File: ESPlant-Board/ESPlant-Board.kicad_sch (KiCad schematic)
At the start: 47 parts, among them J1 Conn_01x05, U1 USB-C, U13 ESP32-C6-MINI-1-N4, U3 AHT20-F, U4 Tactile-Switch, U5 3.3V-Regulator, U6 Light sensor, U7 Tactile-Switch, U8 Slide-Switch, U9 Battery-Spring

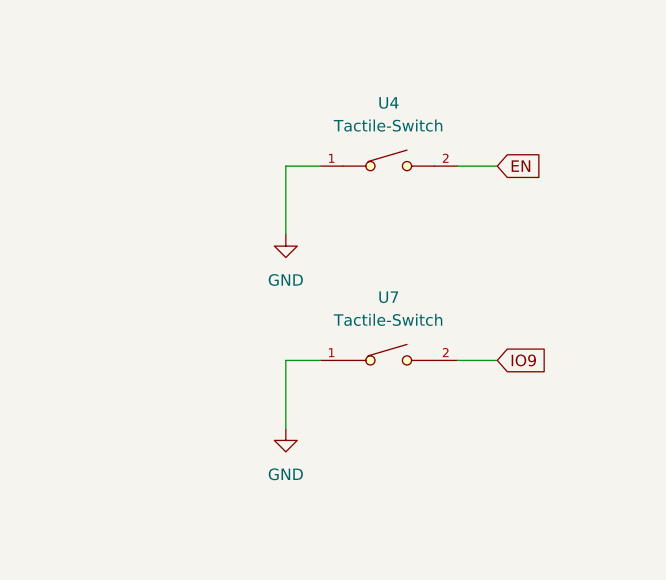
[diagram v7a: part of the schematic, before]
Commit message: Board: Add debouncing caps to buttons
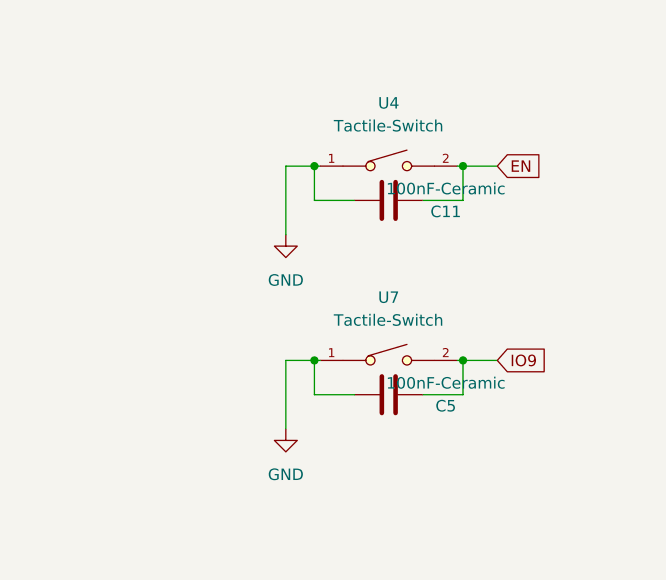
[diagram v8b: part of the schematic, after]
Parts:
- added C11, C5: 100nF-Ceramic, Capacitor_SMD:C_0402_1005Metric, symbol Device:C
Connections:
- net EN: now also C11.1
- net GND: now also C11.2, C5.2
- net IO9: now also C5.1
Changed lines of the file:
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@@
   (junction (at 205.74 81.28) (diameter 0) (color 0 0 0 0)
   )
+  (junction (at 254.635 99.06) (diameter 0) (color 0 0 0 0)
+  )
   (junction (at 205.74 101.6) (diameter 0) (color 0 0 0 0)
   )
@@
   (junction (at 93.345 165.735) (diameter 0) (color 0 0 0 0)
   )
+  (junction (at 254.635 77.47) (diameter 0) (color 0 0 0 0)
+  )
   (junction (at 36.83 175.895) (diameter 0) (color 0 0 0 0)
   )
@@
   (junction (at 31.115 175.895) (diameter 0) (color 0 0 0 0)
   )
+  (junction (at 271.145 99.06) (diameter 0) (color 0 0 0 0)
+  )
   (junction (at 36.83 168.275) (diameter 0) (color 0 0 0 0)
   )
@@
   )
   (junction (at 205.74 99.06) (diameter 0) (color 0 0 0 0)
+  )
+  (junction (at 271.145 77.47) (diameter 0) (color 0 0 0 0)
   )
   (junction (at 70.485 111.76) (diameter 0) (color 0 0 0 0)
@@
     (stroke (width 0) (type default))
   )
+  (wire (pts (xy 271.145 102.87) (xy 271.145 99.06))
+    (stroke (width 0) (type default))
+  )
   (wire (pts (xy 205.74 99.06) (xy 205.74 101.6))
     (stroke (width 0) (type default))
@@
     (stroke (width 0) (type default))
   )
-  (wire (pts (xy 270.51 77.47) (xy 274.955 77.47))
+  (wire (pts (xy 270.51 77.47) (xy 271.145 77.47))
     (stroke (width 0) (type default))
   )
@@
     (stroke (width 0) (type default))
   )
+  (wire (pts (xy 254.635 99.06) (xy 255.27 99.06))
+    (stroke (width 0) (type default))
+  )
   (wire (pts (xy 128.905 188.595) (xy 129.54 188.595))
     (stroke (width 0) (type default))
@@
     (stroke (width 0) (type default))
   )
+  (wire (pts (xy 271.145 81.28) (xy 271.145 77.47))
+    (stroke (width 0) (type default))
+  )
   (wire (pts (xy 252.73 17.78) (xy 256.54 17.78))
     (stroke (width 0) (type default))
@@
     (stroke (width 0) (type default))
   )
+  (wire (pts (xy 254.635 102.87) (xy 254.635 99.06))
+    (stroke (width 0) (type default))
+  )
   (wire (pts (xy 165.1 55.245) (xy 163.83 55.245))
     (stroke (width 0) (type default))
@@
     (stroke (width 0) (type default))
   )
+  (wire (pts (xy 254.635 81.28) (xy 254.635 77.47))
+    (stroke (width 0) (type default))
+  )
   (wire (pts (xy 128.905 173.355) (xy 129.54 173.355))
     (stroke (width 0) (type default))
@@
     (stroke (width 0) (type default))
   )
+  (wire (pts (xy 271.145 77.47) (xy 274.955 77.47))
+    (stroke (width 0) (type default))
+  )
   (wire (pts (xy 64.77 24.13) (xy 64.77 34.29))
     (stroke (width 0) (type default))
@@
     (stroke (width 0) (type default))
   )
+  (wire (pts (xy 271.145 99.06) (xy 274.955 99.06))
+    (stroke (width 0) (type default))
+  )
   (wire (pts (xy 123.825 168.275) (xy 150.495 168.275))
     (stroke (width 0) (type default))
@@
     (stroke (width 0) (type default))
   )
+  (wire (pts (xy 266.7 81.28) (xy 271.145 81.28))
+    (stroke (width 0) (type default))
+  )
+  (wire (pts (xy 259.08 81.28) (xy 254.635 81.28))
+    (stroke (width 0) (type default))
+  )
   (wire (pts (xy 150.495 165.735) (xy 128.905 165.735))
     (stroke (width 0) (type default))
@@
     (stroke (width 0) (type default))
   )
+  (wire (pts (xy 266.7 102.87) (xy 271.145 102.87))
+    (stroke (width 0) (type default))
+  )
   (wire (pts (xy 31.115 167.005) (xy 31.115 168.275))
     (stroke (width 0) (type default))
@@
     (stroke (width 0) (type default))
   )
-  (wire (pts (xy 251.46 99.06) (xy 255.27 99.06))
+  (wire (pts (xy 251.46 99.06) (xy 254.635 99.06))
     (stroke (width 0) (type default))
   )
@@
     (stroke (width 0) (type default))
   )
+  (wire (pts (xy 254.635 77.47) (xy 255.27 77.47))
+    (stroke (width 0) (type default))
+  )
   (wire (pts (xy 88.265 180.34) (xy 87.63 180.34))
     (stroke (width 0) (type default))
@@
     (stroke (width 0) (type default))
   )
+  (wire (pts (xy 259.08 102.87) (xy 254.635 102.87))
+    (stroke (width 0) (type default))
+  )
   (wire (pts (xy 74.295 170.815) (xy 74.295 175.895))
     (stroke (width 0) (type default))
@@
     (stroke (width 0) (type default))
   )
-  (wire (pts (xy 251.46 77.47) (xy 255.27 77.47))
+  (wire (pts (xy 251.46 77.47) (xy 254.635 77.47))
     (stroke (width 0) (type default))
   )
@@
     (stroke (width 0) (type default))
   )
-  (wire (pts (xy 270.51 99.06) (xy 274.955 99.06))
+  (wire (pts (xy 270.51 99.06) (xy 271.145 99.06))
     (stroke (width 0) (type default))
   )
@@
         (path "/fa2a81f8-bf39-4c28-beef-a6fc807c4564"
           (reference "#PWR014") (unit 1)
+        )
+      )
+    )
+  )
+  (symbol (lib_id "Device:C") (at 262.89 81.28 270) (unit 1)
+    (in_bom yes) (on_board yes) (dnp no)
+    (property "Reference" "C11" (at 269.24 82.55 90)
+      (effects (font (size 1.27 1.27)))
+    )
+    (property "Value" "100nF-Ceramic" (at 269.24 80.01 90)
+      (effects (font (size 1.27 1.27)))
+    )
+    (property "Footprint" "Capacitor_SMD:C_0402_1005Metric" (at 259.08 82.2452 0)
+      (effects (font (size 1.27 1.27)) hide)
+    )
+    (property "Datasheet" "~" (at 262.89 81.28 0)
+      (effects (font (size 1.27 1.27)) hide)
+    )
+    (property "LCSC" "C1525" (at 262.89 81.28 0)
+      (effects (font (size 1.27 1.27)) hide)
+    )
+    (property "MPN" "C1525" (at 262.89 81.28 0)
+      (effects (font (size 1.27 1.27)) hide)
+    )
+    (property "JLCPCB Position Offset" "" (at 262.89 81.28 0)
+      (effects (font (size 1.27 1.27)) hide)
+    )
+    (pin "1")
+    (pin "2")
+    (instances
+      (project "ESPlant-Board"
+        (path "/fa2a81f8-bf39-4c28-beef-a6fc807c4564"
+          (reference "C11") (unit 1)
         )
       )
@@
         )
       )
+    )
+  )
+  (symbol (lib_id "Device:C") (at 262.89 102.87 270) (unit 1)
+    (in_bom yes) (on_board yes) (dnp no)
+    (property "Reference" "C5" (at 269.24 104.14 90)
+      (effects (font (size 1.27 1.27)))
+    )
+    (property "Value" "100nF-Ceramic" (at 269.24 101.6 90)
+      (effects (font (size 1.27 1.27)))
+    )
+    (property "Footprint" "Capacitor_SMD:C_0402_1005Metric" (at 259.08 103.8352 0)
+      (effects (font (size 1.27 1.27)) hide)
+    )
+    (property "Datasheet" "~" (at 262.89 102.87 0)
+      (effects (font (size 1.27 1.27)) hide)
+    )
+    (property "LCSC" "C1525" (at 262.89 102.87 0)
+      (effects (font (size 1.27 1.27)) hide)
+    )
+    (property "MPN" "C1525" (at 262.89 102.87 0)
+      (effects (font (size 1.27 1.27)) hide)
+    )
+    (property "JLCPCB Position Offset" "" (at 262.89 102.87 0)
+      (effects (font (size 1.27 1.27)) hide)
+    )
+    (pin "1")
+    (pin "2")
+    (instances
+      (project "ESPlant-Board"
+        (path "/fa2a81f8-bf39-4c28-beef-a6fc807c4564"
+          (reference "C5") (unit 1)
+        )
+      )
